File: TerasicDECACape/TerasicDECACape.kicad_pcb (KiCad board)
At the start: 4 copper layers, 61.3 x 66.3 mm, 36 parts, among them CN1 NASB0-S6701-TS50, CN2 NASB0-S6701-TS50, J1 MiSTer SDRAM Module, J2 USB_A, J3 Conn_01x03_Male, J4 Conn_02x05_Odd_Even, M1 Sipeed Lichee, P8 BeagleBone_Black_Header, P9 BeagleBone_Black_Header, SW1 TS-1187A-B-A-B, SW2 TS-1187A-B-A-B

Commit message: schematic and PCB cosmetics
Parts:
- moved D5 2.79 mm to (157.3, 113.7)
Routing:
- net GND: track 52.3 -> 53.7 mm
- net Net-(C1-Pad1): track 12.4 -> 11.8 mm
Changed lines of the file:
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@@
     (property "Sheetname" "")
     (attr through_hole)
-    (fp_text reference "SW1" (at -3.395 -0.105 90) (layer "F.SilkS")
+    (fp_text reference "SW1" (at 1.701 -3.714 180) (layer "F.SilkS")
       (effects (font (size 0.8 0.8) (thickness 0.15)))
     )
@@
   )
   (footprint "easyeda2kicad:D0402-BI" (layer "F.Cu")
-    (at 154.4701 113.6824 90)
+    (at 157.2641 113.6904 90)
     (property "JLC Part" "Extended Part")
     (property "LCSC Part" "C191267")
@@
     (property "Sheetname" "")
     (attr through_hole)
-    (fp_text reference "D5" (at 0.05 -1.35 90) (layer "F.SilkS")
+    (fp_text reference "D5" (at -0.01 1.016 90) (layer "F.SilkS")
       (effects (font (size 0.5 0.5) (thickness 0.125)))
     )
@@
     (property "Sheetname" "")
     (attr smd)
-    (fp_text reference "C1" (at 2.65 0 90) (layer "F.SilkS")
-      (effects (font (size 1 1) (thickness 0.15)))
+    (fp_text reference "C1" (at -0.02 -0.892 90) (layer "F.SilkS")
+      (effects (font (size 0.5 0.5) (thickness 0.125)))
     )
     (fp_text value "100nF" (at 0 1.16 90) (layer "F.Fab")
@@
   (gr_line (start 114.568628 55.680928) (end 114.4651 119.5324) (layer "Edge.Cuts") (width 0.00254))
   (gr_arc (start 114.568628 55.680928) (mid 114.92071 54.832399) (end 115.7701 54.4824) (layer "Edge.Cuts") (width 0.00254))
-  (gr_text "HPS RESET" (at 148.8821 120.1674) (layer "F.SilkS")
+  (gr_text "HPS\nRESET" (at 160.8201 111.9124) (layer "F.SilkS")
     (effects (font (size 1 1) (thickness 0.25)))
   )
@@
   (segment (start 126.8501 98.7024) (end 127.5701 97.9824) (width 0.25) (layer "F.Cu") (net 1))
   (segment (start 134.3901 103.8324) (end 132.9201 103.8324) (width 0.25) (layer "F.Cu") (net 1))
+  (segment (start 155.8701 113.1324) (end 157.2061 113.1324) (width 0.25) (layer "F.Cu") (net 1))
   (segment (start 133.3701 116.8324) (end 132.8701 116.3324) (width 0.3) (layer "F.Cu") (net 1))
   (segment (start 134.4001 84.1824) (end 135.8701 84.1824) (width 0.25) (layer "F.Cu") (net 1))
@@
   (segment (start 142.2101 69.5224) (end 142.2101 67.5199) (width 1) (layer "F.Cu") (net 1))
   (segment (start 130.6701 63.8324) (end 130.6701 64.7824) (width 0.3) (layer "F.Cu") (net 1))
+  (segment (start 157.2061 113.1324) (end 157.2641 113.1904) (width 0.25) (layer "F.Cu") (net 1))
   (segment (start 134.4001 116.8324) (end 133.3701 116.8324) (width 0.3) (layer "F.Cu") (net 1))
   (segment (start 126.8501 74.9324) (end 126.8501 74.5524) (width 0.25) (layer "F.Cu") (net 1))
@@
   (segment (start 132.60858 75.5324) (end 133.4601 74.68088) (width 0.3) (layer "B.Cu") (net 167))
   (segment (start 155.5651 116.0624) (end 155.5651 115.2174) (width 0.3) (layer "F.Cu") (net 168))
-  (segment (start 154.4701 114.1824) (end 154.4701 114.9674) (width 0.25) (layer "F.Cu") (net 168))
+  (segment (start 156.5421 114.9124) (end 157.2641 114.1904) (width 0.25) (layer "F.Cu") (net 168))
+  (segment (start 155.8701 114.9124) (end 156.5421 114.9124) (width 0.25) (layer "F.Cu") (net 168))
   (segment (start 153.6201 115.3824) (end 154.8851 115.3824) (width 0.3) (layer "F.Cu") (net 168))
   (segment (start 154.8851 115.3824) (end 155.5651 116.0624) (width 0.25) (layer "F.Cu") (net 168))
-  (segment (start 154.4701 114.9674) (end 155.5651 116.0624) (width 0.25) (layer "F.Cu") (net 168))
   (segment (start 155.5651 115.2174) (end 155.8701 114.9124) (width 0.3) (layer "F.Cu") (net 168))
   (segment (start 155.5651 116.0624) (end 162.1651 116.0624) (width 0.3) (layer "F.Cu") (net 168))

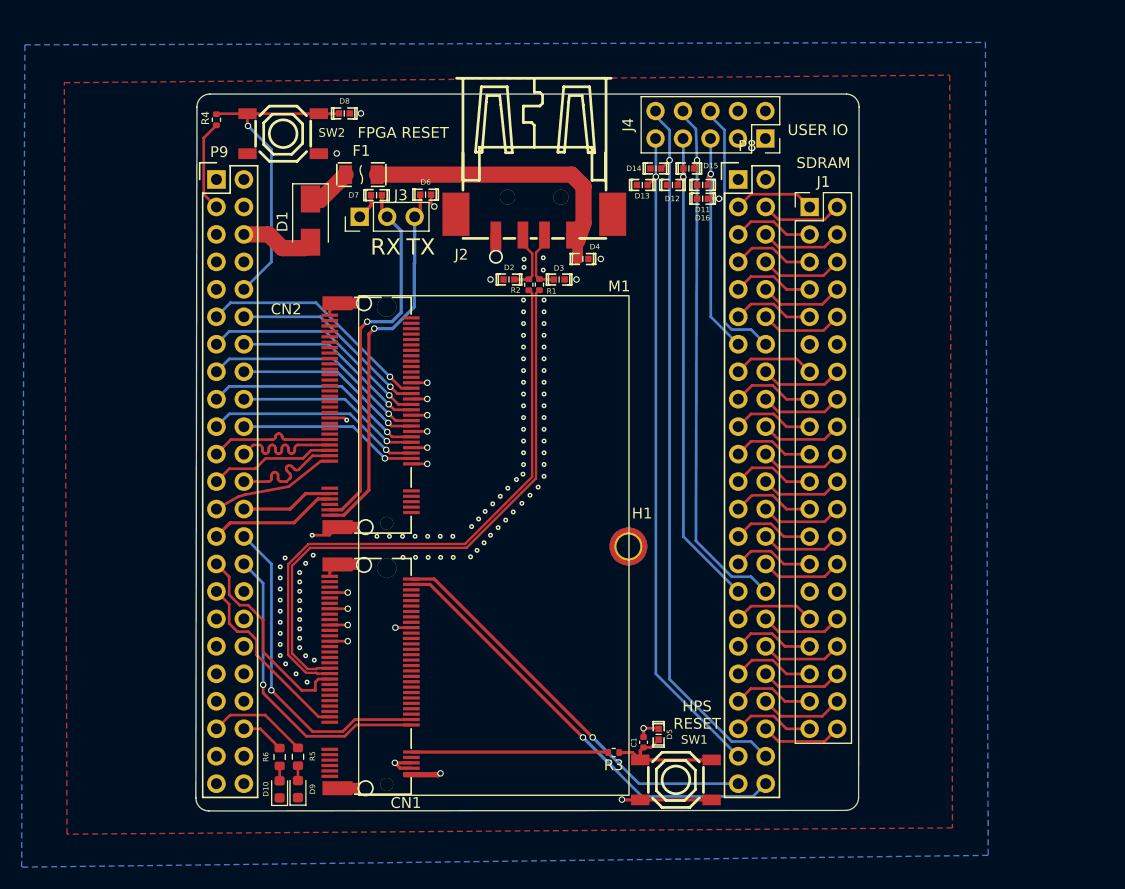
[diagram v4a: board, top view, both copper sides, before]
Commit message: remove LEDs, because we have enough on the base board, add their pins to USER IO
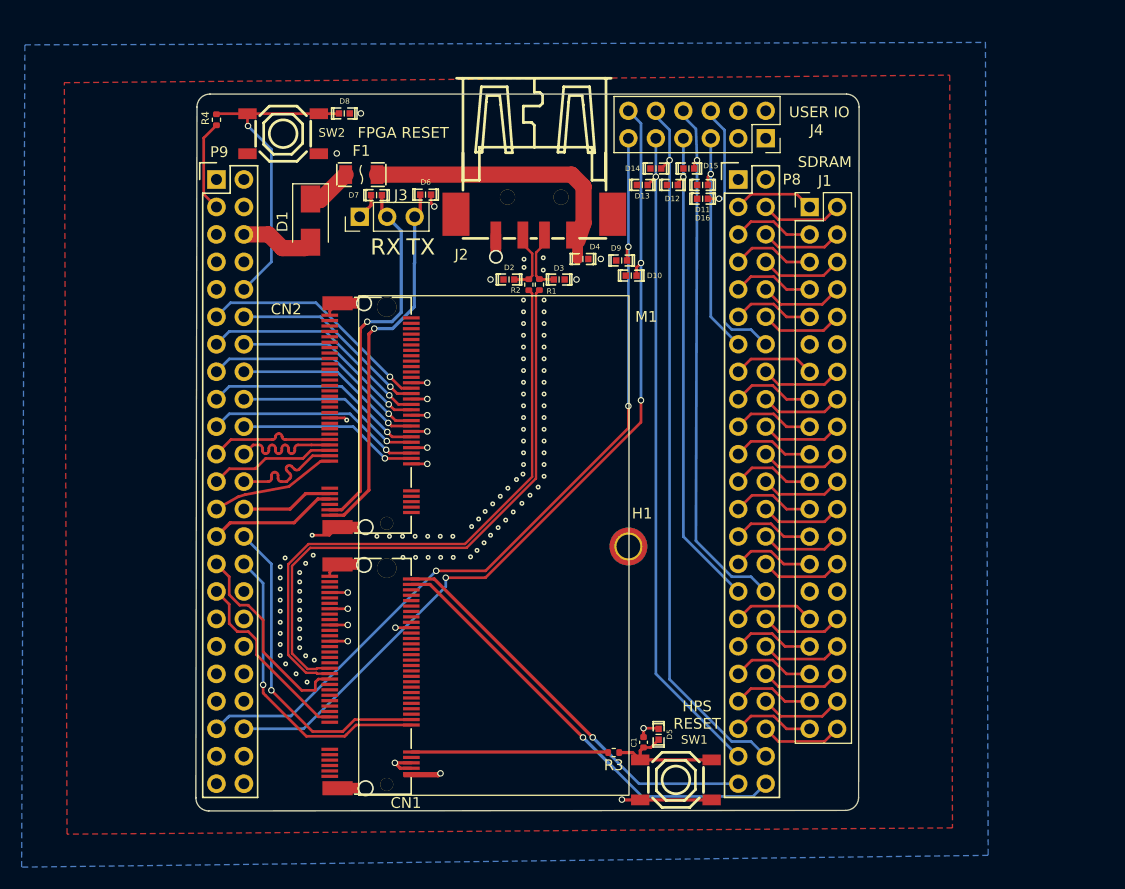
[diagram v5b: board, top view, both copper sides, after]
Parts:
- removed R5, R6: 1k, Resistor_SMD:R_0603_1608Metric
- D10: value red -> LXES15AAA1-133; footprint LED_SMD:LED_0603_1608Metric -> easyeda2kicad:D0402-BI
- D9: value blue -> LXES15AAA1-133; footprint LED_SMD:LED_0603_1608Metric -> easyeda2kicad:D0402-BI
- J4: value Conn_02x05_Odd_Even -> Conn_02x06_Odd_Even; footprint Connector_PinSocket_2.54mm:PinSocket_2x05_P2.54mm_Vertical -> Connector_PinSocket_2.54mm:PinSocket_2x06_P2.54mm_Vertical
- moved D10 57.6 mm to (154.7, 71.3), turned to 180 degrees
- moved D9 57.3 mm to (153.8, 69.9), turned to 180 degrees
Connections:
- D10 pad 1: GND -> /USER7
- D10 pad 2: Net-(R6-Pad1) -> GND
- D9 pad 1: GND -> /USER6
- D9 pad 2: Net-(D9-Pad2) -> GND
- J1 pad 11: unconnected-(J1-Pad11) -> +5V
- P9 pad 41: /LED1 -> /USER6
- P9 pad 42: /LED2 -> /USER7
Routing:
- net /USER7: track 0.00 -> 79.6 mm, vias 0 -> 3
- net /USER6: track 0.00 -> 77.7 mm, vias 0 -> 3
- net +5V: track 84.1 -> 159.4 mm
- net /LED1: track 9.32 -> 0.00 mm
- net /LED2: track 4.04 -> 0.00 mm
- net Net-(R6-Pad1): track 1.38 -> 0.00 mm
- net Net-(D9-Pad2): track 1.38 -> 0.00 mm
